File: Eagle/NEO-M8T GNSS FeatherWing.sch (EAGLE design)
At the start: 31 parts, among them Q1 DMG3415U-7, Q2 2N2222, SW1 KMR2, U1 NEO-M8, X1 uFL

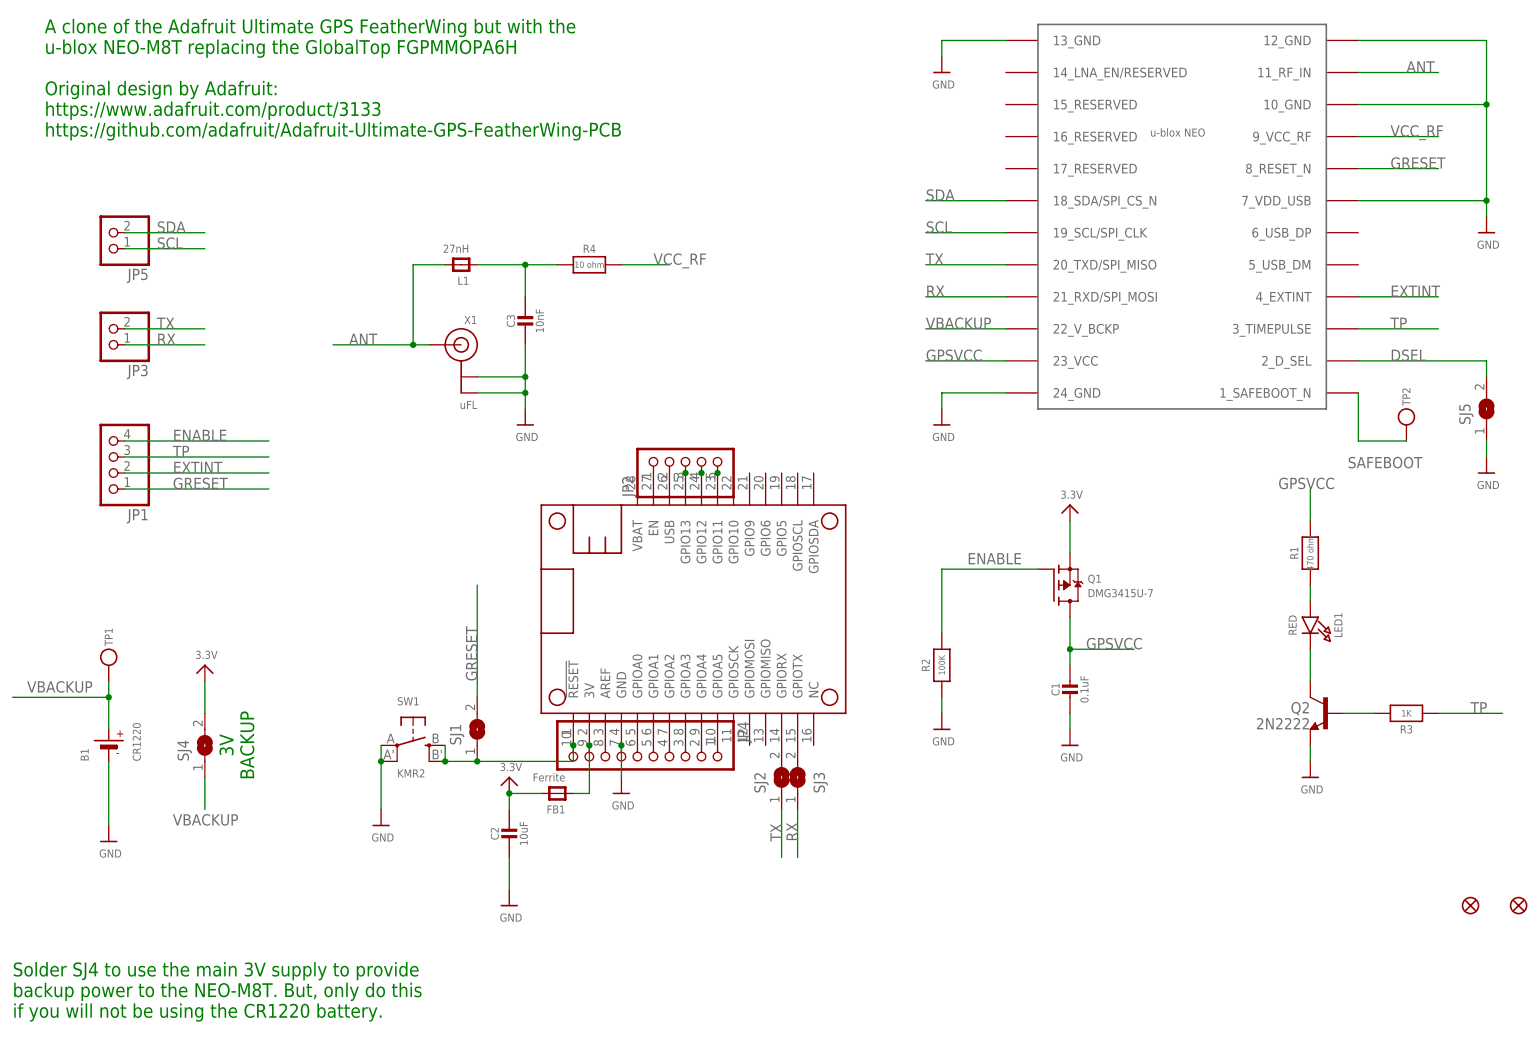
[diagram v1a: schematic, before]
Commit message: Added SCL and SDA pullups
Managed to squeeze in pull-up resistors for SCL and SDA.
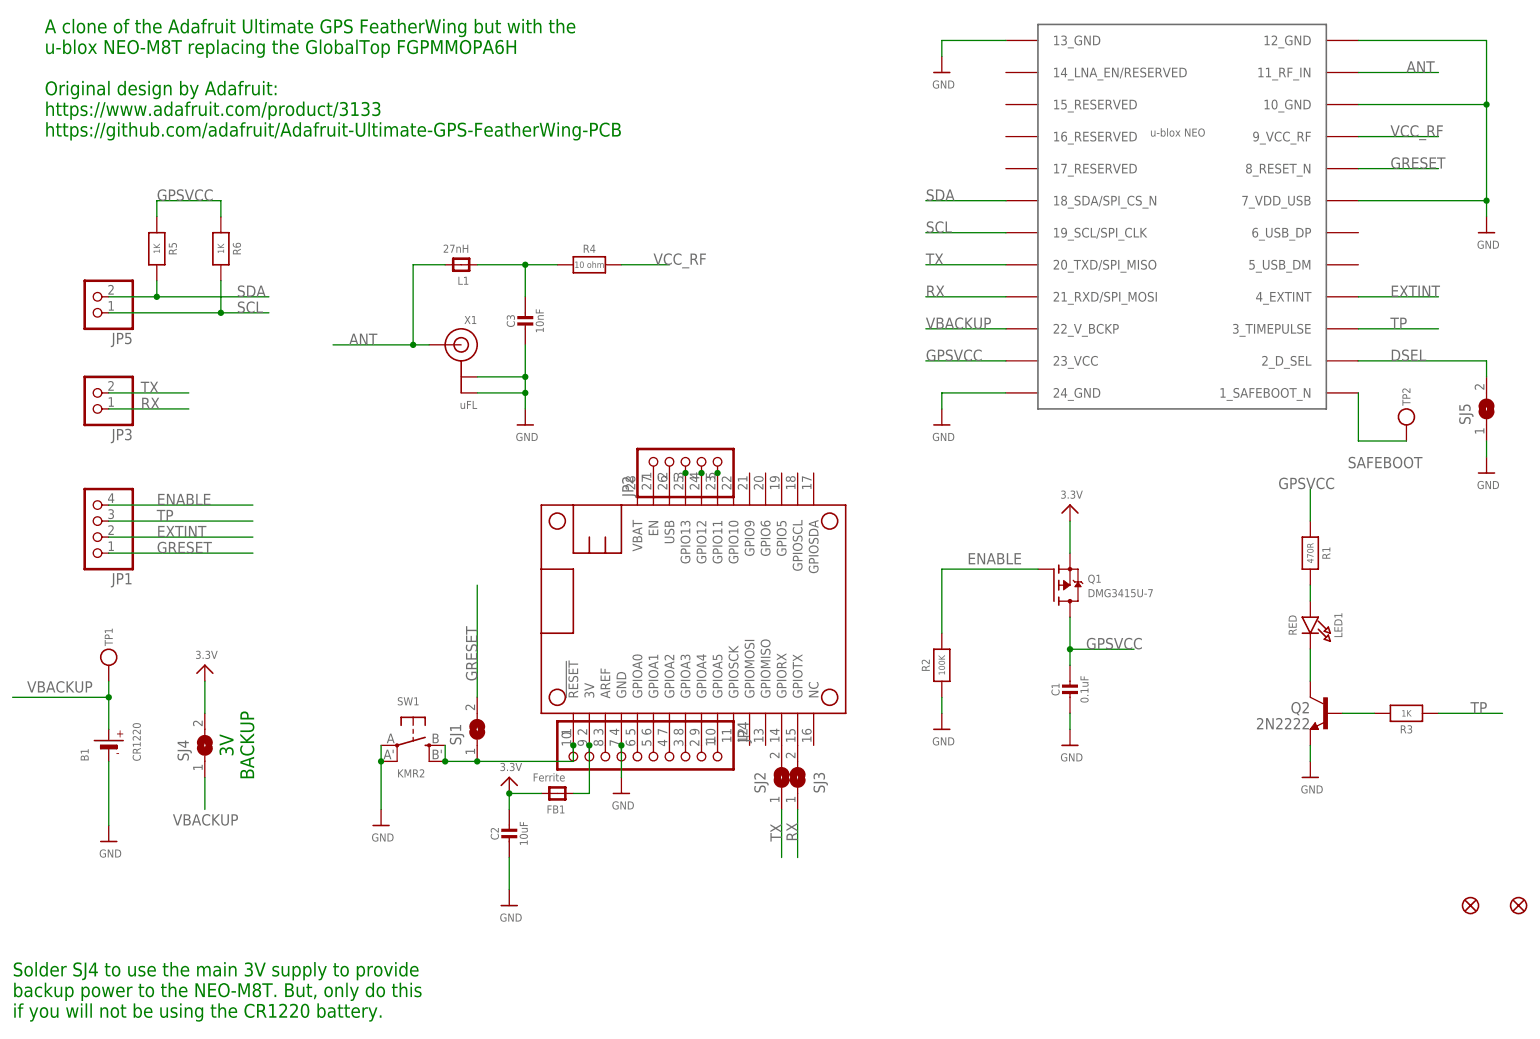
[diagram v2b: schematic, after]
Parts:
- added R5, R6: 1K, microbuilder:RESISTOR_0603_NOOUT
- R1: value 470 ohm -> 470R; device microbuilder:RESISTOR0805_NOOUTLINE -> microbuilder:RESISTOR_0603_NOOUT
- R3: device microbuilder:RESISTOR0805_NOOUTLINE -> microbuilder:RESISTOR_0603_NOOUT
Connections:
- net N$12 renamed RST
- net GPSVCC: now also R1.1, R5.1, R6.1; no longer R1.2
- net N$2: now also R1.2; no longer R1.1
- net SCL: now also R6.2
- net SDA: now also R5.2
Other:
- moved on the sheet: JP1, JP3, JP5, R1
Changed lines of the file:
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@@
 <part name="U$1" library="microbuilder" deviceset="FRAME_A4_ADAFRUIT" device=""/>
 <part name="LED1" library="microbuilder" deviceset="LED" device="0805_NOOUTLINE" value="RED"/>
-<part name="R1" library="microbuilder" deviceset="RESISTOR" device="0805_NOOUTLINE" value="470 ohm"/>
 <part name="U$3" library="microbuilder" deviceset="3.3V" device=""/>
 <part name="U$4" library="microbuilder" deviceset="3.3V" device=""/>
@@
 <part name="Q2" library="transistor" deviceset="*-NPN-" device="SOT23-BEC" technology="MMBT2222ALT1" value="2N2222"/>
 <part name="U$13" library="microbuilder" deviceset="GND" device=""/>
-<part name="R3" library="microbuilder" deviceset="RESISTOR" device="0805_NOOUTLINE" value="1K"/>
 <part name="U$17" library="microbuilder" deviceset="GND" device=""/>
 <part name="R4" library="microbuilder" deviceset="RESISTOR" device="0805_NOOUTLINE" value="10 ohm"/>
@@
 <part name="SJ4" library="microbuilder" deviceset="SOLDERJUMPER" device=""/>
 <part name="TP2" library="microbuilder" deviceset="TESTPOINT" device="ROUND1.5MM"/>
+<part name="R5" library="microbuilder" deviceset="RESISTOR" device="_0603_NOOUT" value="1K"/>
+<part name="R6" library="microbuilder" deviceset="RESISTOR" device="_0603_NOOUT" value="1K"/>
+<part name="R1" library="microbuilder" deviceset="RESISTOR" device="_0603_NOOUT" value="470R"/>
+<part name="R3" library="microbuilder" deviceset="RESISTOR" device="_0603_NOOUT" value="1K"/>
 </parts>
 <sheets>
@@
 <instance part="U$1" gate="G$1" x="0" y="0"/>
 <instance part="LED1" gate="G$1" x="218.44" y="71.12" rot="R270"/>
-<instance part="R1" gate="G$1" x="218.44" y="83.82" rot="R90"/>
 <instance part="U$3" gate="G$1" x="91.44" y="48.26"/>
 <instance part="U$4" gate="G$1" x="180.34" y="91.44"/>
@@
 <instance part="JP2" gate="A" x="119.38" y="99.06" rot="R90"/>
 <instance part="Q1" gate="G$1" x="180.34" y="78.74"/>
-<instance part="JP1" gate="A" x="27.94" y="99.06" rot="R180"/>
+<instance part="JP1" gate="A" x="25.4" y="88.9" rot="R180"/>
 <instance part="R2" gate="G$1" x="160.02" y="66.04" rot="R90"/>
 <instance part="U$7" gate="G$1" x="160.02" y="55.88"/>
-<instance part="JP3" gate="G$1" x="27.94" y="119.38" rot="R180"/>
+<instance part="JP3" gate="G$1" x="25.4" y="109.22" rot="R180"/>
 <instance part="SJ2" gate="1" x="134.62" y="48.26" rot="R90"/>
 <instance part="SJ3" gate="1" x="137.16" y="48.26" rot="MR90"/>
@@
 </instance>
 <instance part="U$13" gate="G$1" x="218.44" y="48.26"/>
-<instance part="R3" gate="G$1" x="233.68" y="58.42" rot="R180"/>
 <instance part="U$17" gate="G$1" x="180.34" y="53.34"/>
 <instance part="R4" gate="G$1" x="104.14" y="129.54"/>
-<instance part="JP5" gate="G$1" x="27.94" y="134.62" rot="R180"/>
+<instance part="JP5" gate="G$1" x="25.4" y="124.46" rot="R180"/>
 <instance part="U$2" gate="G$1" x="43.18" y="66.04"/>
 <instance part="L1" gate="G$1" x="83.82" y="129.54" rot="R180"/>
@@
 <instance part="SJ4" gate="1" x="43.18" y="53.34" rot="R90"/>
 <instance part="TP2" gate="G$1" x="233.68" y="101.6"/>
+<instance part="R5" gate="G$1" x="35.56" y="132.08" rot="R270"/>
+<instance part="R6" gate="G$1" x="45.72" y="132.08" rot="R270"/>
+<instance part="R1" gate="G$1" x="218.44" y="83.82" rot="R270"/>
+<instance part="R3" gate="G$1" x="233.68" y="58.42" rot="R180"/>
 </instances>
 <busses>
@@
 <net name="TX" class="0">
 <segment>
-<wire x1="43.18" y1="119.38" x2="30.48" y2="119.38" width="0.1524" layer="91"/>
-<label x="35.56" y="119.38" size="1.778" layer="95"/>
+<wire x1="40.64" y1="109.22" x2="27.94" y2="109.22" width="0.1524" layer="91"/>
+<label x="33.02" y="109.22" size="1.778" layer="95"/>
 <pinref part="JP3" gate="G$1" pin="2"/>
 </segment>
@@
 <net name="RX" class="0">
 <segment>
-<wire x1="43.18" y1="116.84" x2="30.48" y2="116.84" width="0.1524" layer="91"/>
-<label x="35.56" y="116.84" size="1.778" layer="95"/>
+<wire x1="40.64" y1="106.68" x2="27.94" y2="106.68" width="0.1524" layer="91"/>
+<label x="33.02" y="106.68" size="1.778" layer="95"/>
 <pinref part="JP3" gate="G$1" pin="1"/>
 </segment>
@@
 <net name="GRESET" class="0">
 <segment>
-<wire x1="53.34" y1="93.98" x2="30.48" y2="93.98" width="0.1524" layer="91"/>
-<label x="38.1" y="93.98" size="1.778" layer="95"/>
+<wire x1="50.8" y1="83.82" x2="27.94" y2="83.82" width="0.1524" layer="91"/>
+<label x="35.56" y="83.82" size="1.778" layer="95"/>
 <pinref part="JP1" gate="A" pin="1"/>
 </segment>
@@
 </segment>
 </net>
-<net name="N$12" class="0">
+<net name="RST" class="0">
 <segment>
 <pinref part="SW1" gate="G$1" pin="S"/>
@@
 </segment>
 <segment>
-<pinref part="R1" gate="G$1" pin="2"/>
+<label x="213.36" y="93.98" size="1.778" layer="95"/>
+<pinref part="R1" gate="G$1" pin="1"/>
 <wire x1="218.44" y1="88.9" x2="218.44" y2="93.98" width="0.1524" layer="91"/>
-<label x="213.36" y="93.98" size="1.778" layer="95"/>
 </segment>
 <segment>
@@
 <label x="157.48" y="114.3" size="1.778" layer="95"/>
 </segment>
+<segment>
+<pinref part="R5" gate="G$1" pin="1"/>
+<wire x1="35.56" y1="137.16" x2="35.56" y2="139.7" width="0.1524" layer="91"/>
+<wire x1="35.56" y1="139.7" x2="45.72" y2="139.7" width="0.1524" layer="91"/>
+<pinref part="R6" gate="G$1" pin="1"/>
+<wire x1="45.72" y1="139.7" x2="45.72" y2="137.16" width="0.1524" layer="91"/>
+<label x="35.56" y="139.7" size="1.778" layer="95"/>
+</segment>
 </net>
 <net name="ENABLE" class="0">
 <segment>
 <pinref part="JP1" gate="A" pin="4"/>
-<wire x1="30.48" y1="101.6" x2="53.34" y2="101.6" width="0.1524" layer="91"/>
-<label x="38.1" y="101.6" size="1.778" layer="95"/>
+<wire x1="27.94" y1="91.44" x2="50.8" y2="91.44" width="0.1524" layer="91"/>
+<label x="35.56" y="91.44" size="1.778" layer="95"/>
 </segment>
 <segment>
@@
 <net name="TP" class="0">
 <segment>
+<label x="243.84" y="58.42" size="1.778" layer="95"/>
 <pinref part="R3" gate="G$1" pin="1"/>
 <wire x1="238.76" y1="58.42" x2="248.92" y2="58.42" width="0.1524" layer="91"/>
-<label x="243.84" y="58.42" size="1.778" layer="95"/>
 </segment>
 <segment>
 <pinref part="JP1" gate="A" pin="3"/>
-<wire x1="30.48" y1="99.06" x2="53.34" y2="99.06" width="0.1524" layer="91"/>
-<label x="38.1" y="99.06" size="1.778" layer="95"/>
+<wire x1="27.94" y1="88.9" x2="50.8" y2="88.9" width="0.1524" layer="91"/>
+<label x="35.56" y="88.9" size="1.778" layer="95"/>
 </segment>
 <segment>
@@
 <pinref part="Q2" gate="G$1" pin="B"/>
 <pinref part="R3" gate="G$1" pin="2"/>
-<wire x1="223.52" y1="58.42" x2="228.6" y2="58.42" width="0.1524" layer="91"/>
+<wire x1="228.6" y1="58.42" x2="223.52" y2="58.42" width="0.1524" layer="91"/>
 </segment>
 </net>
@@
 <segment>
 <pinref part="JP1" gate="A" pin="2"/>
-<wire x1="30.48" y1="96.52" x2="53.34" y2="96.52" width="0.1524" layer="91"/>
-<label x="38.1" y="96.52" size="1.778" layer="95"/>
+<wire x1="27.94" y1="86.36" x2="50.8" y2="86.36" width="0.1524" layer="91"/>
+<label x="35.56" y="86.36" size="1.778" layer="95"/>
 </segment>
 <segment>
@@
 <segment>
 <pinref part="LED1" gate="G$1" pin="A"/>
-<pinref part="R1" gate="G$1" pin="1"/>
 <wire x1="218.44" y1="76.2" x2="218.44" y2="78.74" width="0.1524" layer="91"/>
+<pinref part="R1" gate="G$1" pin="2"/>
 </segment>
 </net>
@@
 <segment>
 <pinref part="JP5" gate="G$1" pin="2"/>
-<wire x1="30.48" y1="134.62" x2="43.18" y2="134.62" width="0.1524" layer="91"/>
-<label x="35.56" y="134.62" size="1.778" layer="95"/>
+<wire x1="27.94" y1="124.46" x2="35.56" y2="124.46" width="0.1524" layer="91"/>
+<label x="48.26" y="124.46" size="1.778" layer="95"/>
+<pinref part="R5" gate="G$1" pin="2"/>
+<wire x1="35.56" y1="124.46" x2="53.34" y2="124.46" width="0.1524" layer="91"/>
+<wire x1="35.56" y1="127" x2="35.56" y2="124.46" width="0.1524" layer="91"/>
+<junction x="35.56" y="124.46"/>
 </segment>
 <segment>
@@
 <segment>
 <pinref part="JP5" gate="G$1" pin="1"/>
-<wire x1="30.48" y1="132.08" x2="43.18" y2="132.08" width="0.1524" layer="91"/>
-<label x="35.56" y="132.08" size="1.778" layer="95"/>
-</segment>
-<segment>
+<wire x1="27.94" y1="121.92" x2="45.72" y2="121.92" width="0.1524" layer="91"/>
+<label x="48.26" y="121.92" size="1.778" layer="95"/>
+<pinref part="R6" gate="G$1" pin="2"/>
+<wire x1="45.72" y1="121.92" x2="53.34" y2="121.92" width="0.1524" layer="91"/>
+<wire x1="45.72" y1="127" x2="45.72" y2="121.92" width="0.1524" layer="91"/>
+<junction x="45.72" y="121.92"/>
+</segment>
+<segment>
